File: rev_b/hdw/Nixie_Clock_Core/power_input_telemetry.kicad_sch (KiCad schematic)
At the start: 7 parts, among them U301 INA219BxDCN, U302 MCP9804

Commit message: lots of rev B control board schematic progress
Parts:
- renumbered C302 to C?, C303 to C?, C301 to C?, DOC301 to DOC?, DOC302 to DOC?, U302 to U?, U301 to U?
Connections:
- net POS3P3_SNS- renamed POS24_SNS-

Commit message: more rev b sch progress
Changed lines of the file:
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@@
     (company "Drew Maatman")
   )
-  (junction (at 125.73 59.69) (diameter 0) (color 0 0 0 0)
+  (junction (at 125.73 60.96) (diameter 0) (color 0 0 0 0)
   )
   (junction (at 148.59 132.08) (diameter 0) (color 0 0 0 0)
@@
   )
   (no_connect (at 138.43 118.11))
-  (wire (pts (xy 109.22 59.69) (xy 125.73 59.69))
+  (wire (pts (xy 109.22 60.96) (xy 125.73 60.96))
     (stroke (width 0) (type default))
   )
@@
     (stroke (width 0) (type default))
   )
-  (wire (pts (xy 133.35 59.69) (xy 125.73 59.69))
+  (wire (pts (xy 133.35 60.96) (xy 125.73 60.96))
     (stroke (width 0) (type default))
   )
-  (wire (pts (xy 125.73 59.69) (xy 125.73 58.42))
+  (wire (pts (xy 125.73 58.42) (xy 125.73 60.96))
     (stroke (width 0) (type default))
   )
@@
     (stroke (width 0) (type default))
   )
-  (wire (pts (xy 133.35 57.15) (xy 133.35 59.69))
+  (wire (pts (xy 133.35 57.15) (xy 133.35 60.96))
     (stroke (width 0) (type default))
   )
@@
     )
   )
-  (global_label "POS24_SNS-" (shape passive) (at 109.22 59.69 180)
+  (global_label "POS24_SNS-" (shape passive) (at 109.22 60.96 180)
     (effects (font (size 1.27 1.27)) (justify right))
-    (property "Intersheetrefs" "${INTERSHEET_REFS}" (at 109.22 59.69 0)
+    (property "Intersheetrefs" "${INTERSHEET_REFS}" (at 109.22 60.96 0)
       (effects (font (size 1.27 1.27)) hide)
     )

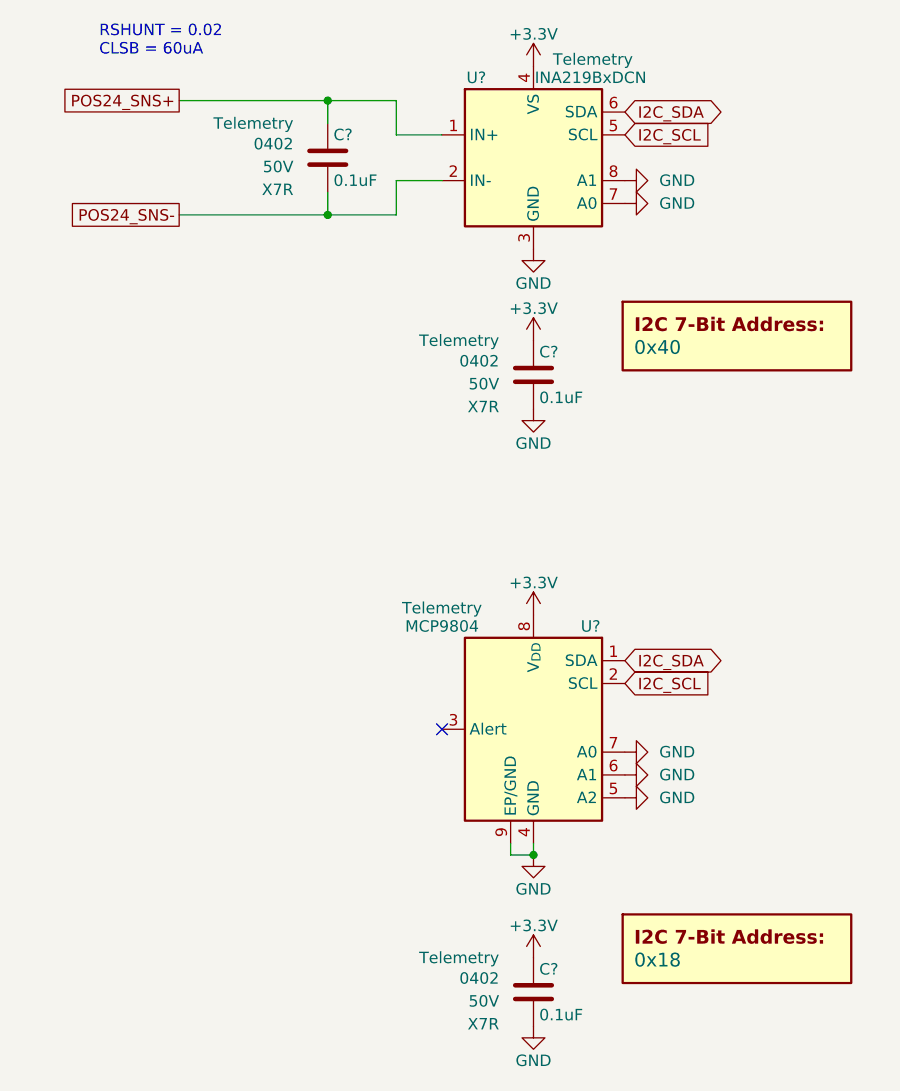
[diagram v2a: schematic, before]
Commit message: updated footprints, ran some DRC
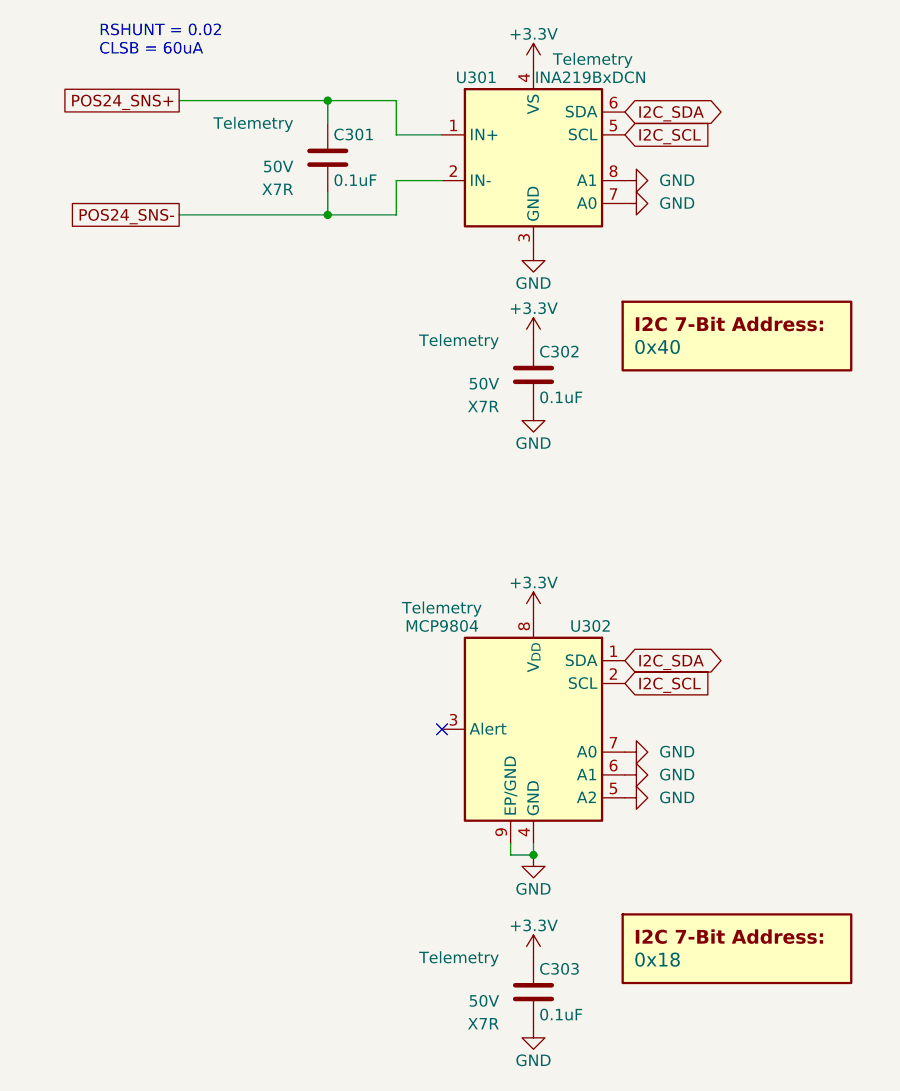
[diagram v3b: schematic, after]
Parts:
- C301, C302, C303: renamed from C?; footprint Capacitors_SMD:C_0402 -> Capacitors_SMD:C_0603; Digi-Key PN 490-10698-1-ND -> (none); display_footprint 0402 -> (none)
- gave numbers to parts that had none: 4

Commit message: hid all passive refdes on core PCB
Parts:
- C301, C302, C303: Digi-Key PN (none) -> 1276-1935-1-ND; display_footprint (none) -> 0603
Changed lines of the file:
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@@
       (effects (font (size 1.27 1.27)) hide)
     )
-    (property "display_footprint" "" (at 144.78 77.216 0)
+    (property "display_footprint" "0603" (at 144.78 77.216 0)
       (effects (font (size 1.27 1.27)) (justify right))
     )
@@
       (effects (font (size 1.27 1.27)) (justify right))
     )
-    (property "Digi-Key PN" "" (at 148.59 78.74 0)
+    (property "Digi-Key PN" "1276-1935-1-ND" (at 148.59 78.74 0)
       (effects (font (size 1.27 1.27)) hide)
     )
@@
       (effects (font (size 1.27 1.27)) hide)
     )
-    (property "display_footprint" "" (at 144.78 145.796 0)
+    (property "display_footprint" "0603" (at 144.78 145.796 0)
       (effects (font (size 1.27 1.27)) (justify right))
     )
@@
       (effects (font (size 1.27 1.27)) (justify right))
     )
-    (property "Digi-Key PN" "" (at 148.59 147.32 0)
+    (property "Digi-Key PN" "1276-1935-1-ND" (at 148.59 147.32 0)
       (effects (font (size 1.27 1.27)) hide)
     )
@@
       (effects (font (size 1.27 1.27)) hide)
     )
-    (property "display_footprint" "" (at 121.92 53.086 0)
+    (property "display_footprint" "0603" (at 121.92 53.086 0)
       (effects (font (size 1.27 1.27)) (justify right))
     )
@@
       (effects (font (size 1.27 1.27)) (justify right))
     )
-    (property "Digi-Key PN" "" (at 125.73 54.61 0)
-      (effects (font (size 1.27 1.27)) hide)
-    )
+    (property "Digi-Key PN" "1276-1935-1-ND" (at 125.73 54.61 0)
+      (effects (font (size 1.27 1.27)) hide)
+    )

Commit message: added BOM
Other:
- title: (none) -> Nixie Clock Redux Core Board
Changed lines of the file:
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@@
   (paper "A")
   (title_block
-    (date "2023-05-12")
-    (rev "PRELIM")
+    (title "Nixie Clock Redux Core Board")
+    (date "2023-07-30")
+    (rev "B")
     (company "Drew Maatman")
   )
@@
     (effects (font (size 1.27 1.27)) (justify left bottom))
   )
-  (global_label "I2C_SDA" (shape bidirectional) (at 158.75 49.53 0)
+  (global_label "I2C_SDA" (shape bidirectional) (at 158.75 49.53 0) (fields_autoplaced)
     (effects (font (size 1.27 1.27)) (justify left))
-    (property "Intersheetrefs" "${INTERSHEET_REFS}" (at 158.75 49.53 0)
-      (effects (font (size 1.27 1.27)) hide)
+    (property "Intersheetrefs" "${INTERSHEET_REFS}" (at 170.3871 49.53 0)
+      (effects (font (size 1.27 1.27)) (justify left))
     )
   )
-  (global_label "POS24_SNS+" (shape passive) (at 109.22 48.26 180)
+  (global_label "POS24_SNS+" (shape passive) (at 109.22 48.26 180) (fields_autoplaced)
     (effects (font (size 1.27 1.27)) (justify right))
-    (property "Intersheetrefs" "${INTERSHEET_REFS}" (at 109.22 48.26 0)
-      (effects (font (size 1.27 1.27)) hide)
+    (property "Intersheetrefs" "${INTERSHEET_REFS}" (at 94.907 48.26 0)
+      (effects (font (size 1.27 1.27)) (justify right))
     )
   )
-  (global_label "POS24_SNS-" (shape passive) (at 109.22 60.96 180)
+  (global_label "POS24_SNS-" (shape passive) (at 109.22 60.96 180) (fields_autoplaced)
     (effects (font (size 1.27 1.27)) (justify right))
-    (property "Intersheetrefs" "${INTERSHEET_REFS}" (at 109.22 60.96 0)
-      (effects (font (size 1.27 1.27)) hide)
+    (property "Intersheetrefs" "${INTERSHEET_REFS}" (at 94.907 60.96 0)
+      (effects (font (size 1.27 1.27)) (justify right))
     )
   )
-  (global_label "I2C_SDA" (shape bidirectional) (at 158.75 110.49 0)
+  (global_label "I2C_SDA" (shape bidirectional) (at 158.75 110.49 0) (fields_autoplaced)
     (effects (font (size 1.27 1.27)) (justify left))
-    (property "Intersheetrefs" "${INTERSHEET_REFS}" (at 158.75 110.49 0)
-      (effects (font (size 1.27 1.27)) hide)
+    (property "Intersheetrefs" "${INTERSHEET_REFS}" (at 170.3871 110.49 0)
+      (effects (font (size 1.27 1.27)) (justify left))
     )
   )
-  (global_label "I2C_SCL" (shape input) (at 158.75 113.03 0)
+  (global_label "I2C_SCL" (shape input) (at 158.75 113.03 0) (fields_autoplaced)
     (effects (font (size 1.27 1.27)) (justify left))
-    (property "Intersheetrefs" "${INTERSHEET_REFS}" (at 158.75 113.03 0)
-      (effects (font (size 1.27 1.27)) hide)
+    (property "Intersheetrefs" "${INTERSHEET_REFS}" (at 169.2153 113.03 0)
+      (effects (font (size 1.27 1.27)) (justify left))
     )
   )
-  (global_label "I2C_SCL" (shape input) (at 158.75 52.07 0)
+  (global_label "I2C_SCL" (shape input) (at 158.75 52.07 0) (fields_autoplaced)
     (effects (font (size 1.27 1.27)) (justify left))
-    (property "Intersheetrefs" "${INTERSHEET_REFS}" (at 158.75 52.07 0)
-      (effects (font (size 1.27 1.27)) hide)
+    (property "Intersheetrefs" "${INTERSHEET_REFS}" (at 169.2153 52.07 0)
+      (effects (font (size 1.27 1.27)) (justify left))
     )
   )
